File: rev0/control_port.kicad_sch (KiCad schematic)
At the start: 22 parts, among them IC1 ECP5-BGA256, U8 USB3343-CP

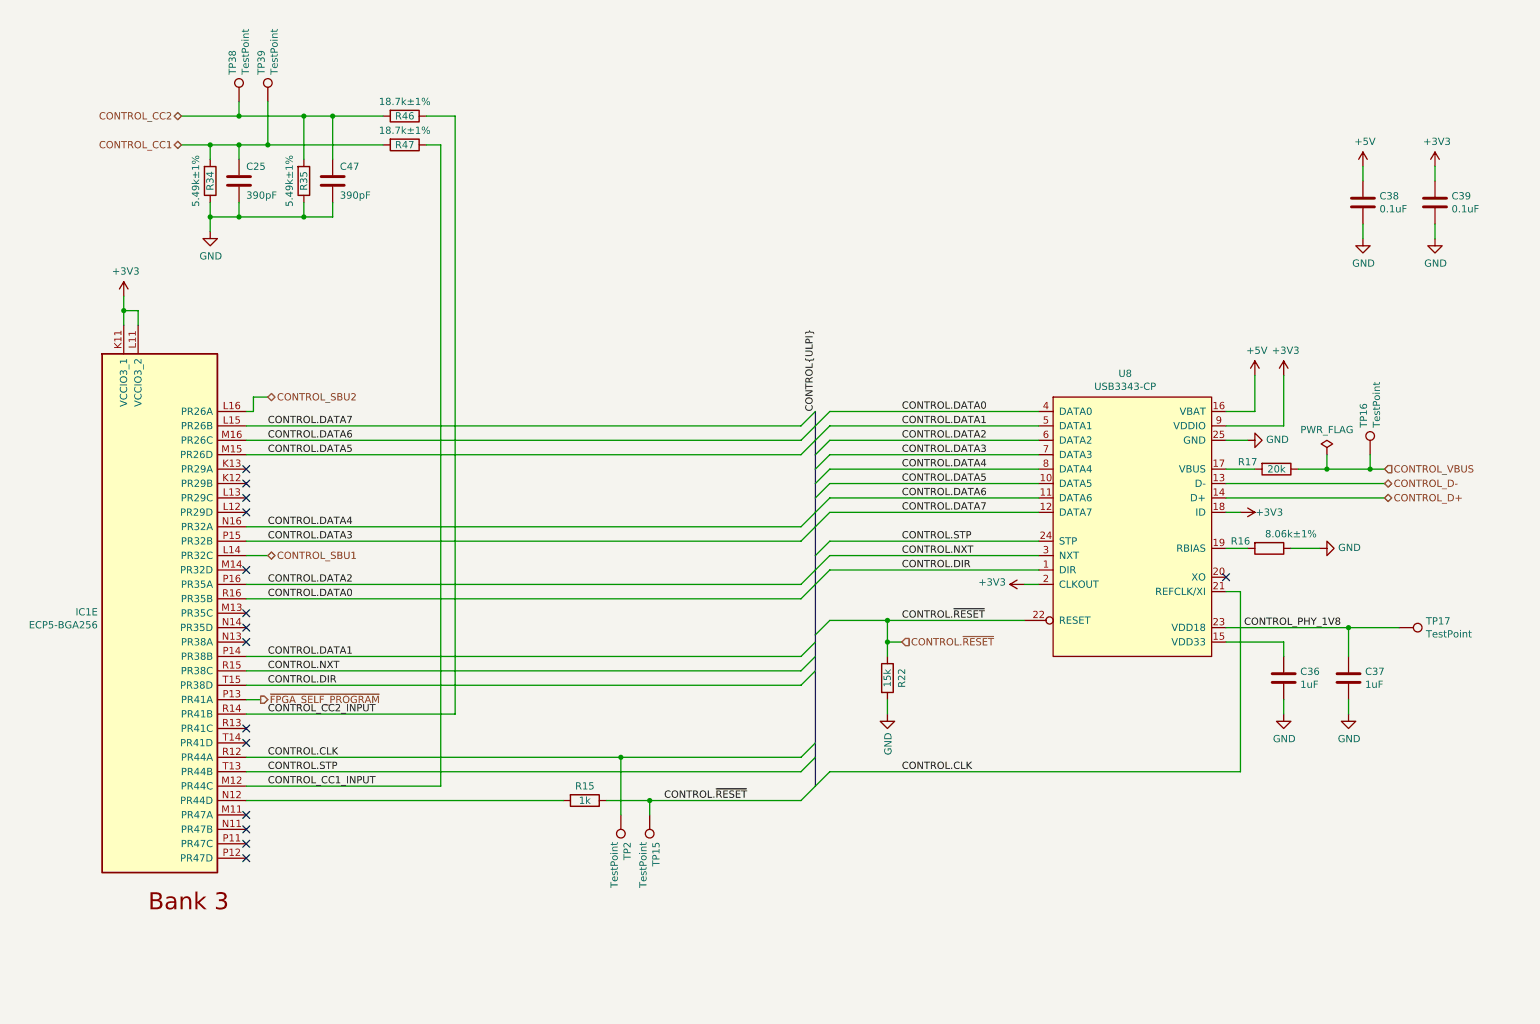
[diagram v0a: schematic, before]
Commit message: hardware: add Control port USB switch
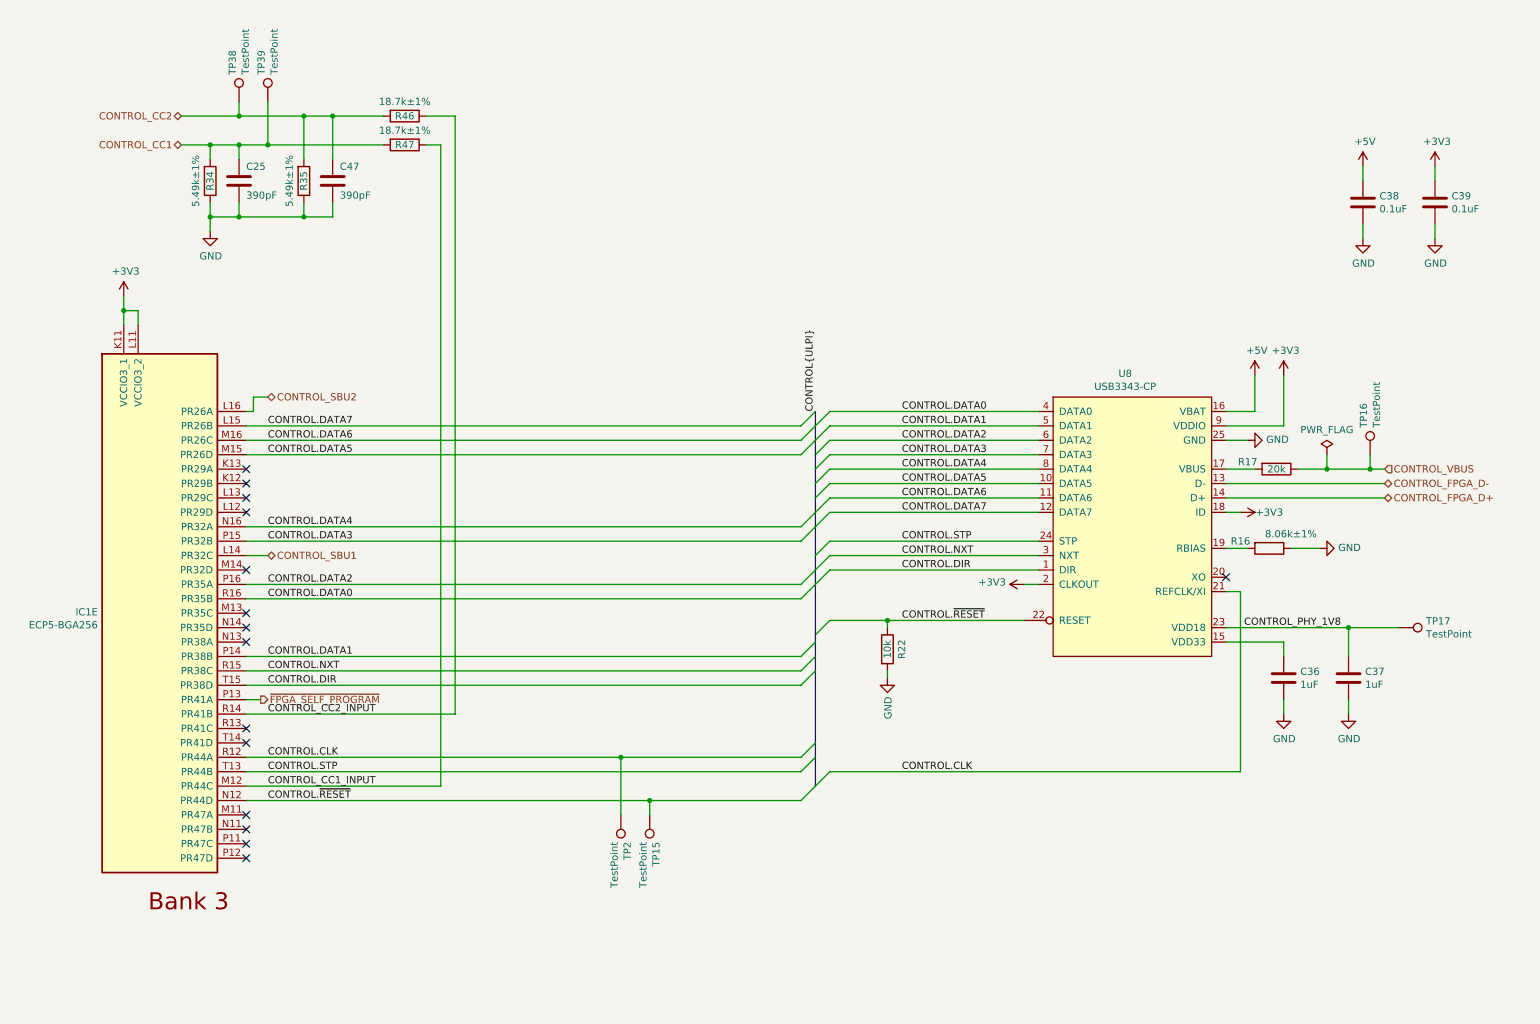
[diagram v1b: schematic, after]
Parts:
- removed R15: 1k, Resistor_SMD:R_0402_1005Metric, symbol Device:R
- R22: value 15k -> 10k; Part Number GENERIC-RES-0402-15K -> GENERIC-RES-0402-10K
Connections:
- net CONTROL.~{RESET}: now also IC1.N12 (PR44D)
- net CONTROL_D+ renamed CONTROL_FPGA_D+
- net CONTROL_D- renamed CONTROL_FPGA_D-
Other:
- moved on the sheet: R22
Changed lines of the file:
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@@
     (comment 1 "Licensed under the CERN-OHL-P v2")
   )
+  (junction (at 52.07 52.07) (diameter 0) (color 0 0 0 0)
+  )
+  (junction (at 63.5 34.29) (diameter 0) (color 0 0 0 0)
+  )
+  (junction (at 251.46 96.52) (diameter 0) (color 0 0 0 0)
+  )
+  (junction (at 52.07 39.37) (diameter 0) (color 0 0 0 0)
+  )
+  (junction (at 57.15 39.37) (diameter 0) (color 0 0 0 0)
+  )
+  (junction (at 68.58 34.29) (diameter 0) (color 0 0 0 0)
+  )
+  (junction (at 243.84 96.52) (diameter 0) (color 0 0 0 0)
+  )
+  (junction (at 119.38 147.32) (diameter 0) (color 0 0 0 0)
+  )
+  (junction (at 31.75 68.58) (diameter 0) (color 0 0 0 0)
+  )
+  (junction (at 46.99 52.07) (diameter 0) (color 0 0 0 0)
+  )
+  (junction (at 166.37 123.19) (diameter 0) (color 0 0 0 0)
+  )
   (junction (at 124.46 154.94) (diameter 0) (color 0 0 0 0)
-  )
-  (junction (at 52.07 52.07) (diameter 0) (color 0 0 0 0)
-  )
-  (junction (at 63.5 34.29) (diameter 0) (color 0 0 0 0)
-  )
-  (junction (at 251.46 96.52) (diameter 0) (color 0 0 0 0)
-  )
-  (junction (at 52.07 39.37) (diameter 0) (color 0 0 0 0)
-  )
-  (junction (at 57.15 39.37) (diameter 0) (color 0 0 0 0)
-  )
-  (junction (at 68.58 34.29) (diameter 0) (color 0 0 0 0)
-  )
-  (junction (at 243.84 96.52) (diameter 0) (color 0 0 0 0)
-  )
-  (junction (at 119.38 147.32) (diameter 0) (color 0 0 0 0)
-  )
-  (junction (at 166.37 127) (diameter 0) (color 0 0 0 0)
-  )
-  (junction (at 31.75 68.58) (diameter 0) (color 0 0 0 0)
-  )
-  (junction (at 46.99 52.07) (diameter 0) (color 0 0 0 0)
-  )
-  (junction (at 166.37 123.19) (diameter 0) (color 0 0 0 0)
   )
   (junction (at 52.07 34.29) (diameter 0) (color 0 0 0 0)
@@
     (stroke (width 0) (type default) (color 0 0 0 0))
   )
-  (wire (pts (xy 166.37 137.16) (xy 166.37 139.7))
+  (wire (pts (xy 166.37 132.08) (xy 166.37 133.35))
     (stroke (width 0) (type default) (color 0 0 0 0))
   )
@@
     (stroke (width 0) (type default) (color 0 0 0 0))
   )
-  (wire (pts (xy 109.22 154.94) (xy 53.34 154.94))
+  (wire (pts (xy 124.46 154.94) (xy 53.34 154.94))
     (stroke (width 0) (type default) (color 0 0 0 0))
   )
@@
     (stroke (width 0) (type default) (color 0 0 0 0))
   )
-  (wire (pts (xy 166.37 127) (xy 168.91 127))
-    (stroke (width 0) (type default) (color 0 0 0 0))
-  )
   (wire (pts (xy 226.06 86.36) (xy 231.14 86.36))
     (stroke (width 0) (type default) (color 0 0 0 0))
@@
     (stroke (width 0) (type default) (color 0 0 0 0))
   )
-  (wire (pts (xy 166.37 127) (xy 166.37 129.54))
+  (wire (pts (xy 166.37 123.19) (xy 166.37 124.46))
     (stroke (width 0) (type default) (color 0 0 0 0))
   )
@@
     (stroke (width 0) (type default) (color 0 0 0 0))
   )
-  (wire (pts (xy 166.37 123.19) (xy 166.37 127))
-    (stroke (width 0) (type default) (color 0 0 0 0))
-  )
   (bus (pts (xy 153.67 101.6) (xy 153.67 104.14))
     (stroke (width 0) (type default) (color 0 0 0 0))
@@
     (stroke (width 0) (type default) (color 0 0 0 0))
   )
-  (wire (pts (xy 116.84 154.94) (xy 124.46 154.94))
-    (stroke (width 0) (type default) (color 0 0 0 0))
-  )
   (wire (pts (xy 68.58 49.53) (xy 68.58 52.07))
     (stroke (width 0) (type default) (color 0 0 0 0))
@@
     (effects (font (size 1.27 1.27)) (justify left bottom))
   )
-  (label "CONTROL.~{RESET}" (at 127 154.94 0)
+  (label "CONTROL.~{RESET}" (at 57.15 154.94 0)
     (effects (font (size 1.27 1.27)) (justify left bottom))
   )
@@
     (effects (font (size 1.27 1.27)) (justify right))
   )
-  (hierarchical_label "CONTROL.~{RESET}" (shape input) (at 168.91 127 0)
-    (effects (font (size 1.27 1.27)) (justify left))
-  )
   (hierarchical_label "CONTROL_SBU2" (shape bidirectional) (at 57.15 83.82 0)
     (effects (font (size 1.27 1.27)) (justify left))
@@
     (effects (font (size 1.27 1.27)) (justify left))
   )
-  (hierarchical_label "CONTROL_D+" (shape bidirectional) (at 254 101.6 0)
+  (hierarchical_label "CONTROL_FPGA_D+" (shape bidirectional) (at 254 101.6 0)
     (effects (font (size 1.27 1.27)) (justify left))
   )
@@
     (effects (font (size 1.27 1.27)) (justify left))
   )
-  (hierarchical_label "CONTROL_D-" (shape bidirectional) (at 254 99.06 0)
+  (hierarchical_label "CONTROL_FPGA_D-" (shape bidirectional) (at 254 99.06 0)
     (effects (font (size 1.27 1.27)) (justify left))
   )
@@
     (pin "1")
   )
-  (symbol (lib_id "Device:R") (at 113.03 154.94 270) (unit 1)
-    (in_bom yes) (on_board yes)
-    (property "Reference" "R15" (id 0) (at 113.03 152.4 90))
-    (property "Value" "1k" (id 1) (at 113.03 154.94 90))
-    (property "Footprint" "Resistor_SMD:R_0402_1005Metric" (id 2) (at 113.03 153.162 90)
-      (effects (font (size 1.27 1.27)) hide)
-    )
-    (property "Datasheet" "~" (id 3) (at 113.03 154.94 0)
-      (effects (font (size 1.27 1.27)) hide)
-    )
-    (property "Part Number" "GENERIC-RES-0402-1K" (id 4) (at 113.03 154.94 0)
-      (effects (font (size 1.27 1.27)) hide)
-    )
-    (property "Substitution" "any equivalent" (id 5) (at 113.03 154.94 0)
+  (symbol (lib_id "Device:R") (at 166.37 128.27 0) (unit 1)
+    (in_bom yes) (on_board yes)
+    (property "Reference" "R22" (id 0) (at 168.91 128.27 90))
+    (property "Value" "10k" (id 1) (at 166.37 128.27 90))
+    (property "Footprint" "Resistor_SMD:R_0402_1005Metric" (id 2) (at 164.592 128.27 90)
+      (effects (font (size 1.27 1.27)) hide)
+    )
+    (property "Datasheet" "~" (id 3) (at 166.37 128.27 0)
+      (effects (font (size 1.27 1.27)) hide)
+    )
+    (property "Part Number" "GENERIC-RES-0402-10K" (id 4) (at 166.37 128.27 0)
+      (effects (font (size 1.27 1.27)) hide)
+    )
+    (property "Substitution" "any equivalent" (id 5) (at 166.37 128.27 0)
       (effects (font (size 1.27 1.27)) hide)
     )
@@
     (pin "2")
   )
-  (symbol (lib_id "Device:R") (at 166.37 133.35 0) (unit 1)
-    (in_bom yes) (on_board yes)
-    (property "Reference" "R22" (id 0) (at 168.91 133.35 90))
-    (property "Value" "15k" (id 1) (at 166.37 133.35 90))
-    (property "Footprint" "Resistor_SMD:R_0402_1005Metric" (id 2) (at 164.592 133.35 90)
-      (effects (font (size 1.27 1.27)) hide)
-    )
-    (property "Datasheet" "~" (id 3) (at 166.37 133.35 0)
-      (effects (font (size 1.27 1.27)) hide)
-    )
-    (property "Part Number" "GENERIC-RES-0402-15K" (id 4) (at 166.37 133.35 0)
-      (effects (font (size 1.27 1.27)) hide)
-    )
-    (property "Substitution" "any equivalent" (id 5) (at 166.37 133.35 0)
-      (effects (font (size 1.27 1.27)) hide)
-    )
-    (pin "1")
-    (pin "2")
-  )
-  (symbol (lib_id "power:GND") (at 166.37 139.7 0) (unit 1)
-    (in_bom yes) (on_board yes)
-    (property "Reference" "#PWR0101" (id 0) (at 166.37 146.05 0)
-      (effects (font (size 1.27 1.27)) hide)
-    )
-    (property "Value" "GND" (id 1) (at 166.497 142.9512 90)
+  (symbol (lib_id "power:GND") (at 166.37 133.35 0) (unit 1)
+    (in_bom yes) (on_board yes)
+    (property "Reference" "#PWR0101" (id 0) (at 166.37 139.7 0)
+      (effects (font (size 1.27 1.27)) hide)
+    )
+    (property "Value" "GND" (id 1) (at 166.497 136.6012 90)
       (effects (font (size 1.27 1.27)) (justify right))
     )
-    (property "Footprint" "" (id 2) (at 166.37 139.7 0)
-      (effects (font (size 1.27 1.27)) hide)
-    )
-    (property "Datasheet" "" (id 3) (at 166.37 139.7 0)
-      (effects (font (size 1.27 1.27)) hide)
-    )
+    (property "Footprint" "" (id 2) (at 166.37 133.35 0)
+      (effects (font (size 1.27 1.27)) hide)
+    )
+    (property "Datasheet" "" (id 3) (at 166.37 133.35 0)
+      (effects (font (size 1.27 1.27)) hide)
+    )

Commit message: hardware: add Control port reset detection
USB reset can be detected by measuring the D+/D- common-mode voltage
with the microcontroller's ADC or analog comparator.
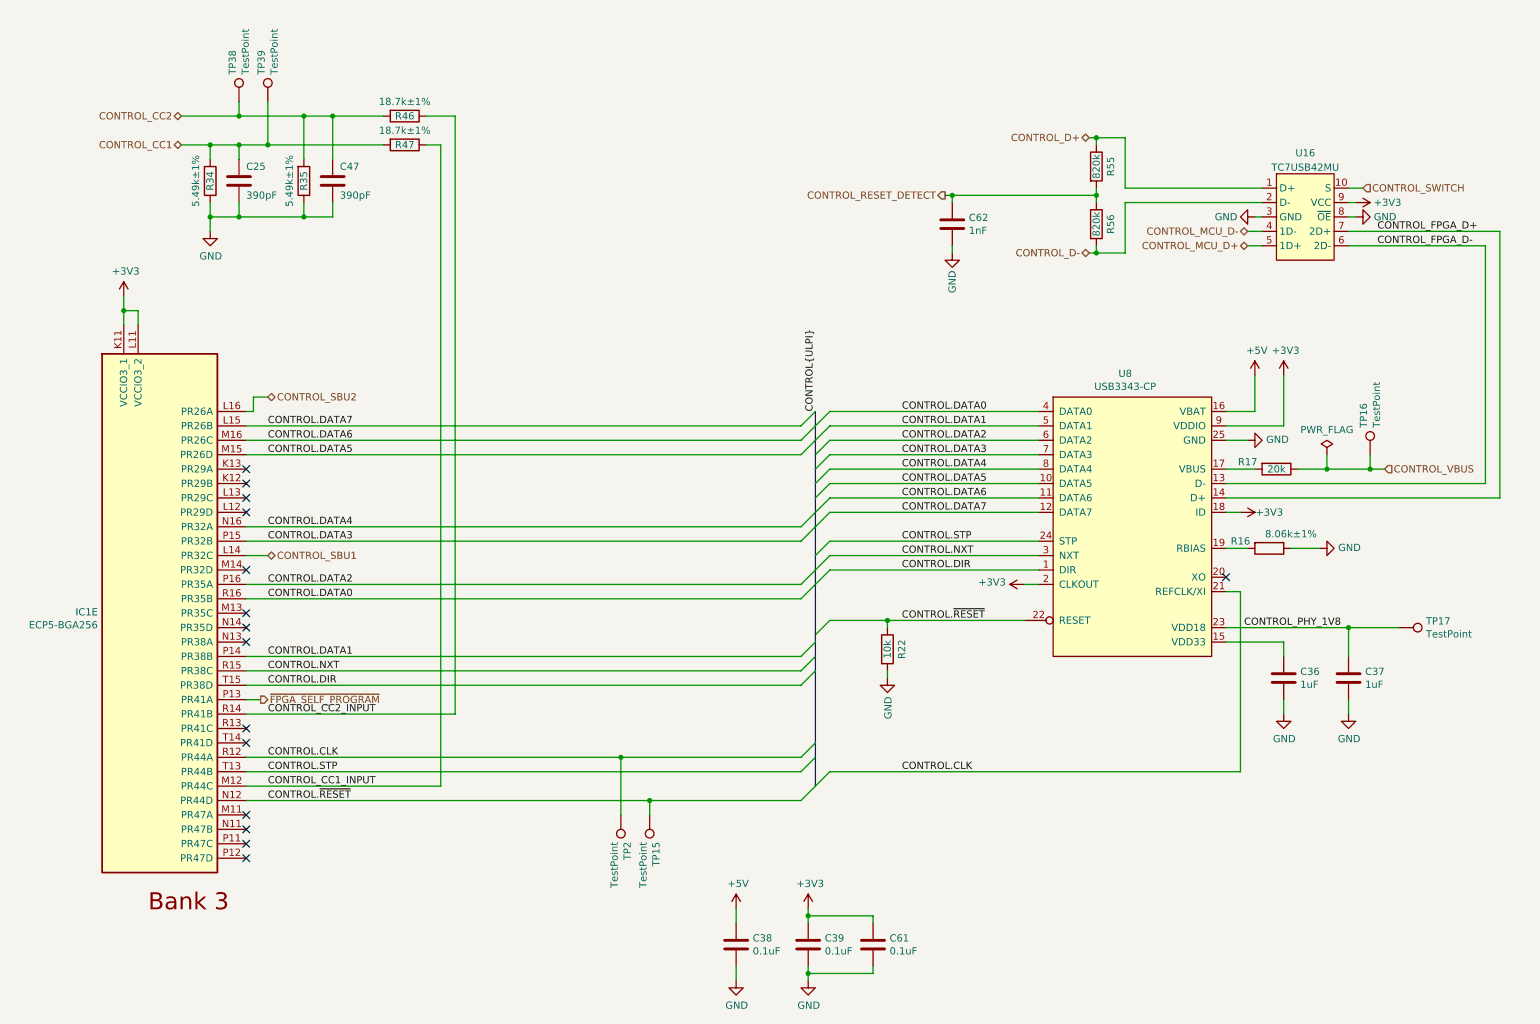
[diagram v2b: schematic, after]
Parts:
- added C61: 0.1uF, Capacitor_SMD:C_0402_1005Metric, symbol Device:C
- added C62: 1nF, Capacitor_SMD:C_0402_1005Metric, symbol Device:C
- added R55, R56: 820k, Resistor_SMD:R_0402_1005Metric, symbol Device:R
- added U16: TC7USB42MU, symbol usb:TC7USB42MU
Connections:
- net +3V3: now also C61.1, U16.9 (VCC)
- net CONTROL_FPGA_D+: now also U16.7 (2D+)
- net CONTROL_FPGA_D-: now also U16.6 (2D-)
- net GND: now also C61.2, C62.2, U16.3 (GND), U16.8 (~{OE})
- new net CONTROL_D+: R55.1, U16.1 (D+)
- new net CONTROL_D-: R56.2, U16.2 (D-)
- new net CONTROL_MCU_D+: U16.5 (1D+)
- new net CONTROL_MCU_D-: U16.4 (1D-)
- new net CONTROL_RESET_DETECT: C62.1, R55.2, R56.1
- new net CONTROL_SWITCH: U16.10 (S)
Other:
- moved on the sheet: C38, C39
